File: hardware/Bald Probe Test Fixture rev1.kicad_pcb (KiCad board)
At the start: 2 copper layers, 48.3 x 15.2 mm, 2 parts, among them J1 SMA_IN, J2 SMA_OUT

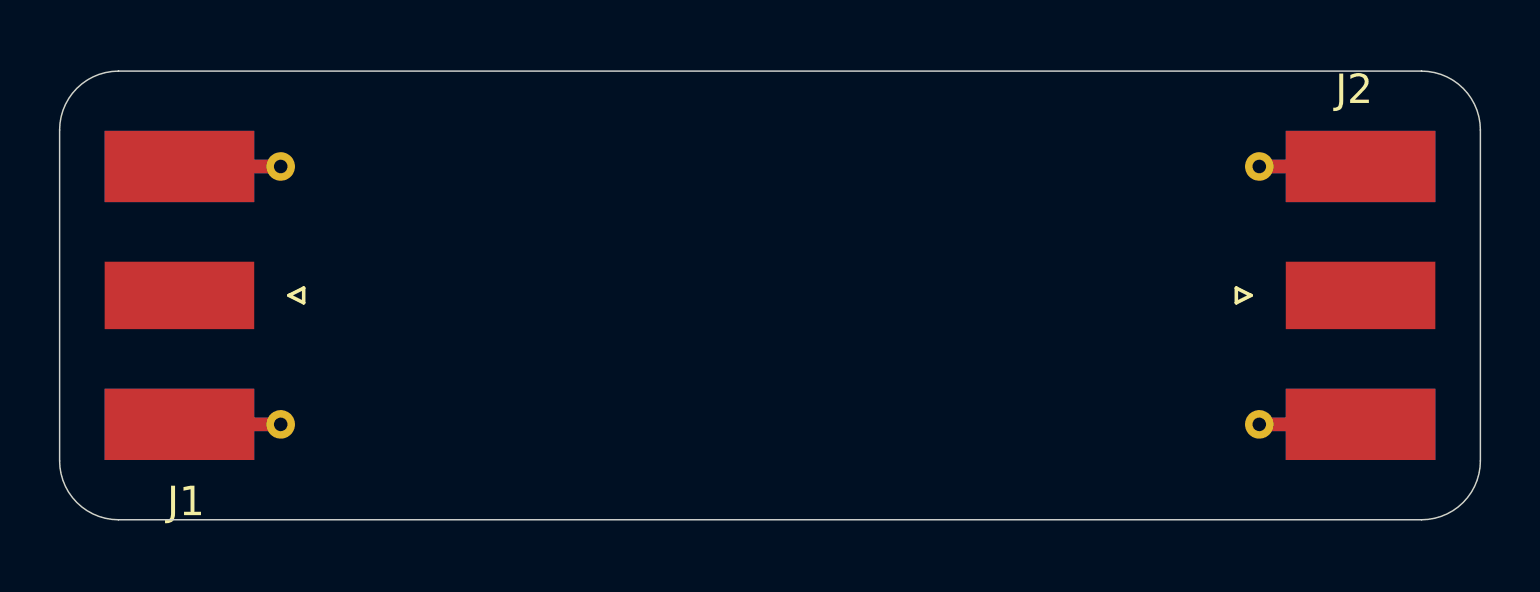
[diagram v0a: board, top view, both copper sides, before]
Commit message: added oshpark 4-layer stackup details
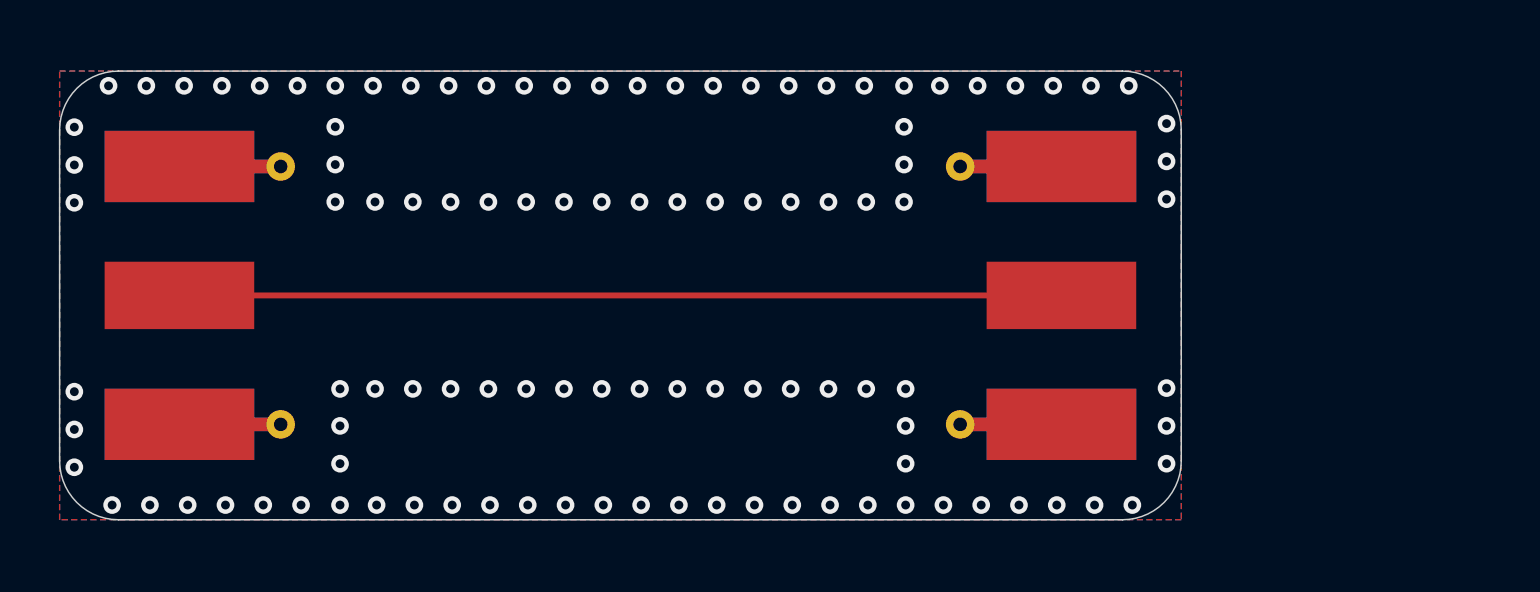
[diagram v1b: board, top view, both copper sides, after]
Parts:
- moved J2 10.2 mm to (141.5, 94.0)
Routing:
- net /thru_trace: track 0.00 -> 30.0 mm
- net GND: vias 0 -> 108
- added copper zone on B.Cu, net GND
- added copper zone on F.Cu, net GND
- added copper zone on In1.Cu, net GND
- added copper zone on In2.Cu, net GND
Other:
- board size 48.3 x 15.2 mm -> 38.1 x 15.2 mm
- copper layers 2 -> 4
- rule pad_to_mask_clearance: 0 -> 0.0508

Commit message: changed to oshpark after dark (2-layer)
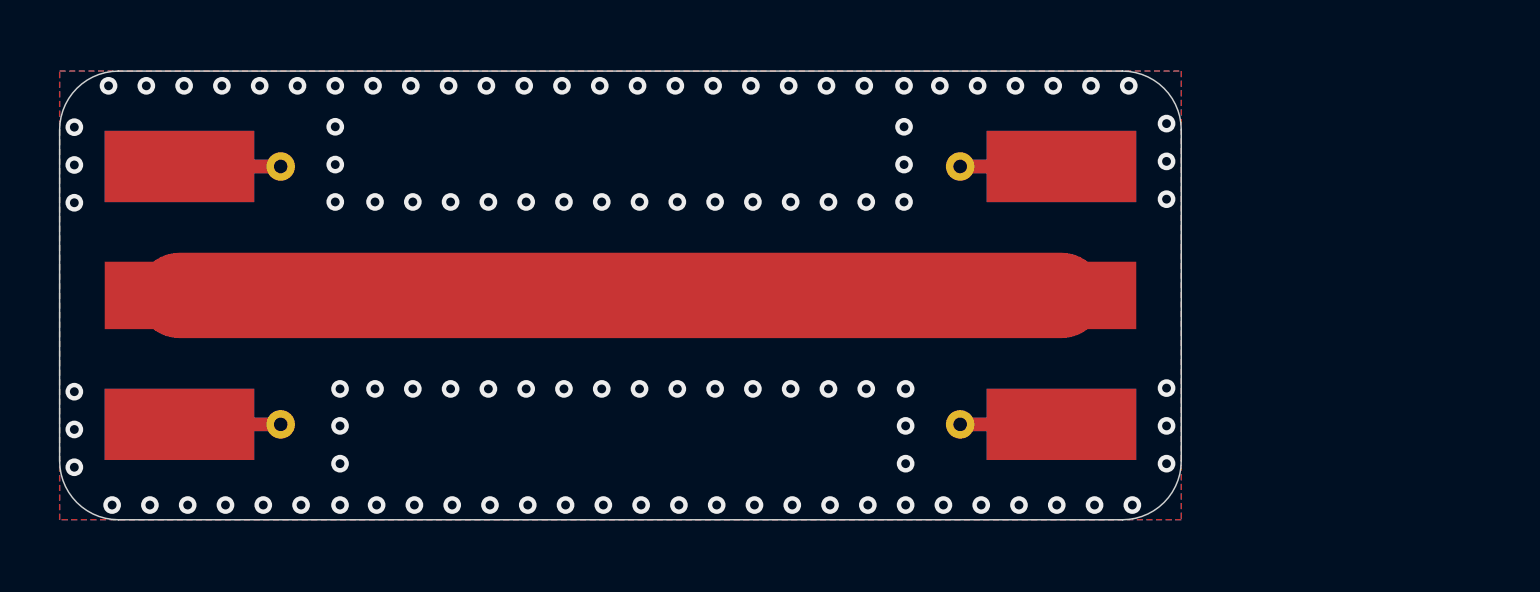
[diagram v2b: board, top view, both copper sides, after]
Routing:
- removed copper zone on In1.Cu, net GND
- removed copper zone on In2.Cu, net GND
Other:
- copper layers 4 -> 2
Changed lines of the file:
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@@
 	(generator_version "8.0")
 	(general
-		(thickness 1.6)
+		(thickness 1.646)
 		(legacy_teardrops no)
 	)
@@
 	(layers
 		(0 "F.Cu" signal)
-		(1 "In1.Cu" signal)
-		(2 "In2.Cu" signal)
 		(31 "B.Cu" signal)
 		(32 "B.Adhes" user "B.Adhesive")
@@
 				(type "Top Silk Screen")
 				(color "White")
+				(material "Direct Printing")
 			)
 			(layer "F.Paste"
@@
 			(layer "F.Mask"
 				(type "Top Solder Mask")
-				(color "Purple")
-				(thickness 0.01)
+				(color "#80808000")
+				(thickness 0.0254)
+				(material "Epoxy")
+				(epsilon_r 3.3)
+				(loss_tangent 0)
 			)
 			(layer "F.Cu"
 				(type "copper")
-				(thickness 0.035)
+				(thickness 0.0356)
 			)
 			(layer "dielectric 1"
-				(type "prepreg")
-				(color "FR4 natural")
-				(thickness 0.1)
-				(material "FR4")
-				(epsilon_r 4.5)
-				(loss_tangent 0.02)
-			)
-			(layer "In1.Cu"
-				(type "copper")
-				(thickness 0.035)
-			)
-			(layer "dielectric 2"
 				(type "core")
 				(color "FR4 natural")
-				(thickness 1.24)
+				(thickness 1.524)
 				(material "FR4")
-				(epsilon_r 4.5)
-				(loss_tangent 0.02)
-			)
-			(layer "In2.Cu"
-				(type "copper")
-				(thickness 0.035)
-			)
-			(layer "dielectric 3"
-				(type "prepreg")
-				(color "FR4 natural")
-				(thickness 0.1)
-				(material "FR4")
-				(epsilon_r 4.5)
-				(loss_tangent 0.02)
+				(epsilon_r 4.35)
+				(loss_tangent 0.013)
 			)
 			(layer "B.Cu"
 				(type "copper")
-				(thickness 0.035)
+				(thickness 0.0356)
 			)
 			(layer "B.Mask"
 				(type "Bottom Solder Mask")
-				(color "Purple")
-				(thickness 0.01)
+				(color "#80808000")
+				(thickness 0.0254)
+				(material "Epoxy")
+				(epsilon_r 3.3)
+				(loss_tangent 0)
 			)
 			(layer "B.Paste"
@@
 				(type "Bottom Silk Screen")
 				(color "White")
+				(material "Direct Printing")
 			)
 			(copper_finish "ENIG")
@@
 		(start 113.29 93.98)
 		(end 143.25 93.98)
-		(width 0.2)
+		(width 2.9)
 		(layer "F.Cu")
 		(net 2)
@@
 		(net 1)
 		(net_name "GND")
-		(layers "F.Cu" "In1.Cu" "In2.Cu" "B.Cu")
+		(layers "F&B.Cu")
 		(hatch edge 0.5)
 		(connect_pads yes
@@
 		(min_thickness 0.1524)
 		(filled_areas_thickness no)
-		(fill
+		(fill yes
 			(thermal_gap 0.5)
 			(thermal_bridge_width 0.5)
@@
 		(polygon
 			(pts
-				(xy 108.458 91.44) (xy 158.242 91.44) (xy 158.242 92.456) (xy 108.458 92.456)
+				(xy 107.7214 80.3656) (xy 157.5054 80.3656) (xy 157.5054 81.3816) (xy 107.7214 81.3816)
 			)
 		)
@@
 		(polygon
 			(pts
-				(xy 108.458 95.504) (xy 158.242 95.504) (xy 158.242 96.52) (xy 108.458 96.52)
-			)
-		)
+				(xy 107.7214 84.4296) (xy 157.5054 84.4296) (xy 157.5054 85.4456) (xy 107.7214 85.4456)
+			)
+		)

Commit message: rev1 ready for fab
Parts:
- added kibuzzard-66881A8D: G***, kibuzzard-66881A8D, B.Cu at (128.3, 94.0)
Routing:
- net /thru_trace: track 30.0 -> 31.5 mm
